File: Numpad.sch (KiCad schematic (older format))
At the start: 68 parts, among them J1 SWD, J2 USB4085-GF-A_REVA, SW1 SW_Push, SW10 SW_Push, SW11 SW_Push, SW12 SW_Push, SW13 SW_Push, SW14 SW_Push, SW15 SW_Push, SW16 SW_Push, SW17 SW_Push, SW18 SW_Push, SW19 SW_Push, SW2 SW_Push, SW20 SW_Push, SW21 SW_Push, SW3 SW_Push, SW4 SW_Push, SW5 SW_Push, SW6 SW_Push, SW7 SW_Push, SW8 SW_Push, SW9 SW_Push, U1 SRV05-4, U2 STM32F103C8Tx, U3 XC6206PxxxMR, Y1 8MHz

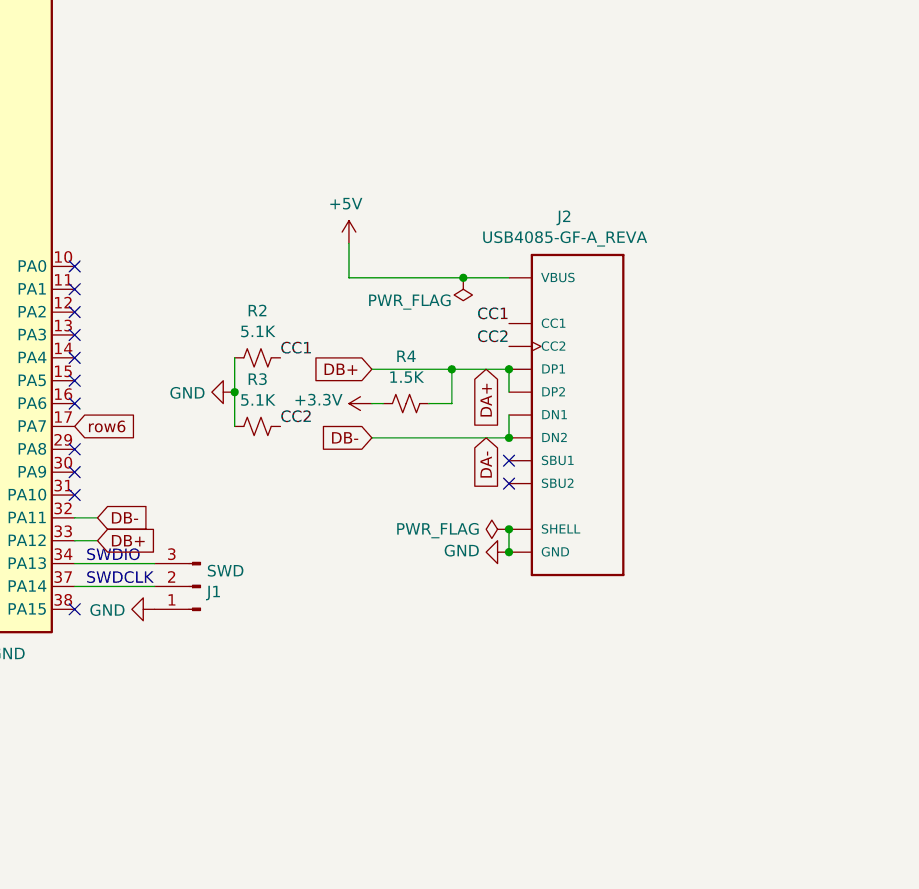
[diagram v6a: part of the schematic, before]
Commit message: 0.3: removed dependencies on external libraries
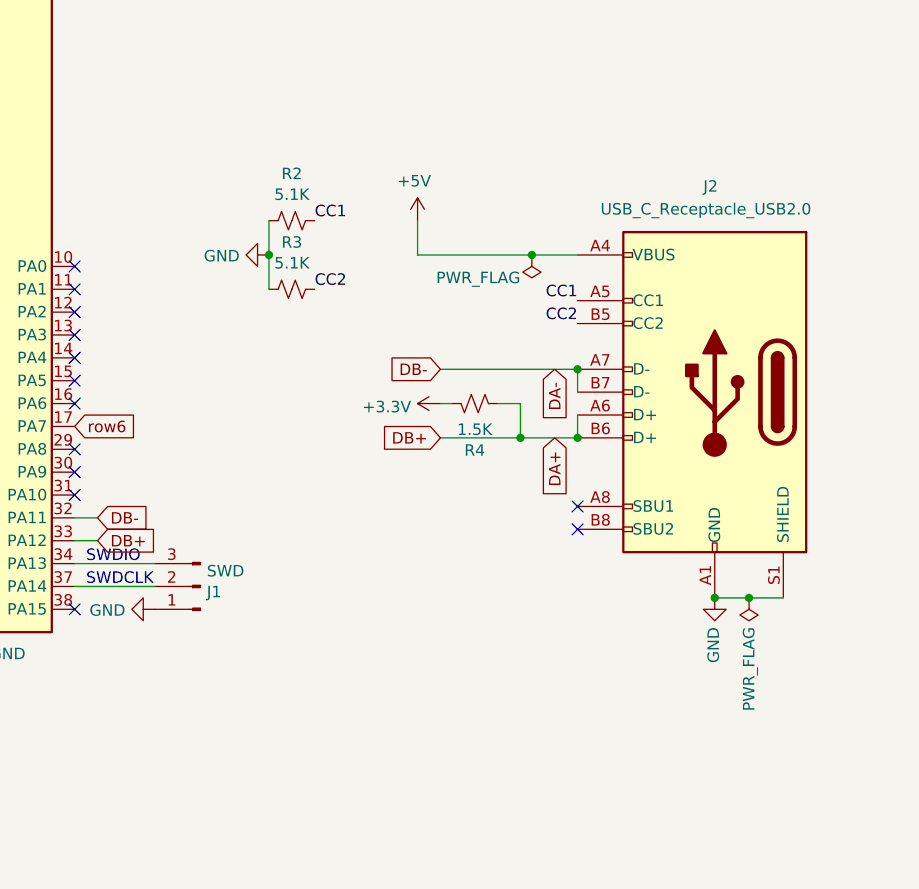
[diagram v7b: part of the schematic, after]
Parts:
- removed J2: USB4085-GF-A_REVA, USB4085:GCT_USB4085-GF-A_REVA, symbol USB4085:USB4085-GF-A_REVA
- added J2: USB_C_Receptacle_USB2.0, Connector_USB:USB_C_Receptacle_GCT_USB4085, symbol Connector:USB_C_Receptacle_USB2.0
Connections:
- net +5V: now also J2.A4 (VBUS), J2.A9 (VBUS), J2.B4 (VBUS), J2.B9 (VBUS)
- net CC1: now also J2.A5 (CC1)
- net CC2: now also J2.B5 (CC2)
- net DA+: now also J2.A6 (D+), J2.B6 (D+)
- net DA-: now also J2.A7 (D-), J2.B7 (D-)
- net GND: now also J2.A1 (GND), J2.A12 (GND), J2.B1 (GND), J2.B12 (GND), J2.S1 (SHIELD)
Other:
- moved on the sheet: R2, R3, R4
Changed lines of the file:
@@
 Text Notes 7700 4600 0    50   ~ 0
 SWDCLK
-$Comp
-L USB4085:USB4085-GF-A_REVA J2
-U 1 1 5E3F05FE
-P 9850 3850
-F 0 "J2" H 9793 4717 50  0000 C CNN
-F 1 "USB4085-GF-A_REVA" H 9793 4626 50  0000 C CNN
-F 2 "USB4085:GCT_USB4085-GF-A_REVA" H 9850 3850 50  0001 L BNN
-F 3 "Global Connector Technology" H 9850 3850 50  0001 L BNN
-F 4 "A" H 9850 3850 50  0001 L BNN "Field4"
-F 5 "Manufacturer Recommendations" H 9850 3850 50  0001 L BNN "Field5"
-	1    9850 3850
-	1    0    0    -1
-$EndComp
-Wire Wire Line
-	8850 3250 8850 3100
+Wire Wire Line
+	9150 3150 9150 3000
 $Comp
 L power:+5V #PWR020
 U 1 1 5E4261EB
-P 8850 3100
-F 0 "#PWR020" H 8850 2950 50  0001 C CNN
-F 1 "+5V" H 8865 3273 50  0000 C CNN
-F 2 "" H 8850 3100 50  0001 C CNN
-F 3 "" H 8850 3100 50  0001 C CNN
-	1    8850 3100
+P 9150 3000
+F 0 "#PWR020" H 9150 2850 50  0001 C CNN
+F 1 "+5V" H 9165 3173 50  0000 C CNN
+F 2 "" H 9150 3000 50  0001 C CNN
+F 3 "" H 9150 3000 50  0001 C CNN
+	1    9150 3000
 	-1   0    0    -1
 $EndComp
-Wire Wire Line
-	9550 3650 9550 3750
-Wire Wire Line
-	9550 3850 9550 3950
 $Comp
 L power:GND #PWR022
 U 1 1 5E42FBA1
-P 9550 4450
-F 0 "#PWR022" H 9550 4200 50  0001 C CNN
-F 1 "GND" V 9555 4322 50  0000 R CNN
-F 2 "" H 9550 4450 50  0001 C CNN
-F 3 "" H 9550 4450 50  0001 C CNN
-	1    9550 4450
-	0    1    -1   0
+P 10450 4650
+F 0 "#PWR022" H 10450 4400 50  0001 C CNN
+F 1 "GND" V 10455 4522 50  0000 R CNN
+F 2 "" H 10450 4650 50  0001 C CNN
+F 3 "" H 10450 4650 50  0001 C CNN
+	1    10450 4650
+	-1   0    0    -1
 $EndComp
 $Comp
 L Device:R_Small_US R2
 U 1 1 5E4574F8
-P 8450 3600
-F 0 "R2" V 8245 3600 50  0000 C CNN
-F 1 "5.1K" V 8336 3600 50  0000 C CNN
-F 2 "Resistor_SMD:R_0402_1005Metric" H 8450 3600 50  0001 C CNN
-F 3 "~" H 8450 3600 50  0001 C CNN
-F 4 "C25905" H 8450 3600 50  0001 C CNN "LCSC"
-	1    8450 3600
+P 8600 3000
+F 0 "R2" V 8395 3000 50  0000 C CNN
+F 1 "5.1K" V 8486 3000 50  0000 C CNN
+F 2 "Resistor_SMD:R_0402_1005Metric" H 8600 3000 50  0001 C CNN
+F 3 "~" H 8600 3000 50  0001 C CNN
+F 4 "C25905" H 8600 3000 50  0001 C CNN "LCSC"
+	1    8600 3000
 	0    1    1    0
 $EndComp
@@
 L power:GND #PWR018
 U 1 1 5E484A5F
-P 8350 3750
-F 0 "#PWR018" H 8350 3500 50  0001 C CNN
-F 1 "GND" V 8355 3622 50  0000 R CNN
-F 2 "" H 8350 3750 50  0001 C CNN
-F 3 "" H 8350 3750 50  0001 C CNN
-	1    8350 3750
+P 8500 3150
+F 0 "#PWR018" H 8500 2900 50  0001 C CNN
+F 1 "GND" V 8505 3022 50  0000 R CNN
+F 2 "" H 8500 3150 50  0001 C CNN
+F 3 "" H 8500 3150 50  0001 C CNN
+	1    8500 3150
 	0    1    1    0
 $EndComp
@@
 NoConn ~ 7650 4100
 NoConn ~ 7650 4200
-NoConn ~ 9550 4050
-NoConn ~ 9550 4150
-Wire Wire Line
-	9550 4350 9550 4450
-Connection ~ 9550 4450
 $Comp
 L Device:R_Small_US R3
 U 1 1 5E458E16
-P 8450 3900
-F 0 "R3" V 8655 3900 50  0000 C CNN
-F 1 "5.1K" V 8564 3900 50  0000 C CNN
-F 2 "Resistor_SMD:R_0402_1005Metric" H 8450 3900 50  0001 C CNN
-F 3 "~" H 8450 3900 50  0001 C CNN
-F 4 "C25905" H 8450 3900 50  0001 C CNN "LCSC"
-	1    8450 3900
+P 8600 3300
+F 0 "R3" V 8805 3300 50  0000 C CNN
+F 1 "5.1K" V 8714 3300 50  0000 C CNN
+F 2 "Resistor_SMD:R_0402_1005Metric" H 8600 3300 50  0001 C CNN
+F 3 "~" H 8600 3300 50  0001 C CNN
+F 4 "C25905" H 8600 3300 50  0001 C CNN "LCSC"
+	1    8600 3300
 	0    -1   -1   0
 $EndComp
@@
 	10200 850  10200 1050
 Wire Wire Line
-	8350 3600 8350 3750
-Wire Wire Line
-	8350 3750 8350 3900
-Connection ~ 8350 3750
-Text Label 8550 3600 0    50   ~ 0
+	8500 3000 8500 3150
+Wire Wire Line
+	8500 3150 8500 3300
+Connection ~ 8500 3150
+Text Label 8700 3000 0    50   ~ 0
 CC1
-Text Label 8550 3900 0    50   ~ 0
+Text Label 8700 3300 0    50   ~ 0
 CC2
-Text Label 9550 3450 2    50   ~ 0
+Text Label 9850 3350 2    50   ~ 0
 CC1
-Text Label 9550 3550 2    50   ~ 0
+Text Label 9850 3450 2    50   ~ 0
 CC2
-Connection ~ 9550 3650
-Connection ~ 9550 3950
 Wire Wire Line
 	7750 4300 7650 4300
@@
 L power:PWR_FLAG #FLG0102
 U 1 1 5E5DCDDC
-P 9550 4350
-F 0 "#FLG0102" H 9550 4425 50  0001 C CNN
-F 1 "PWR_FLAG" V 9550 4477 50  0000 L CNN
-F 2 "" H 9550 4350 50  0001 C CNN
-F 3 "~" H 9550 4350 50  0001 C CNN
-	1    9550 4350
-	0    -1   -1   0
-$EndComp
-Connection ~ 9550 4350
+P 10600 4650
+F 0 "#FLG0102" H 10600 4725 50  0001 C CNN
+F 1 "PWR_FLAG" V 10600 4777 50  0000 L CNN
+F 2 "" H 10600 4650 50  0001 C CNN
+F 3 "~" H 10600 4650 50  0001 C CNN
+	1    10600 4650
+	-1   0    0    1
+$EndComp
 $Comp
 L power:PWR_FLAG #FLG0101
 U 1 1 5E5DC168
-P 9350 3250
-F 0 "#FLG0101" H 9350 3325 50  0001 C CNN
-F 1 "PWR_FLAG" H 9400 3350 50  0000 L CNN
-F 2 "" H 9350 3250 50  0001 C CNN
-F 3 "~" H 9350 3250 50  0001 C CNN
-	1    9350 3250
+P 9650 3150
+F 0 "#FLG0101" H 9650 3225 50  0001 C CNN
+F 1 "PWR_FLAG" H 9700 3250 50  0000 L CNN
+F 2 "" H 9650 3150 50  0001 C CNN
+F 3 "~" H 9650 3150 50  0001 C CNN
+	1    9650 3150
 	-1   0    0    1
 $EndComp
 Wire Wire Line
-	9350 3250 9550 3250
+	9650 3150 9850 3150
 Wire Wire Line
 	6350 2450 6000 2450
@@
 	1    0    0    -1
 $EndComp
-Text GLabel 9450 3650 3    50   Input ~ 0
+Text GLabel 9750 3950 3    50   Input ~ 0
 DA+
-Text GLabel 9450 3950 3    50   Input ~ 0
+Text GLabel 9750 3650 3    50   Input ~ 0
 DA-
-Text GLabel 8950 3650 0    50   Input ~ 0
+Text GLabel 9250 3950 0    50   Input ~ 0
 DB+
-Text GLabel 8950 3950 0    50   Input ~ 0
+Text GLabel 9250 3650 0    50   Input ~ 0
 DB-
 Text GLabel 7750 4300 2    50   Input ~ 0
@@
 DB+
 Wire Wire Line
-	9350 3250 8850 3250
-Connection ~ 9350 3250
-Wire Wire Line
-	8950 3650 9300 3650
-Wire Wire Line
-	8950 3950 9550 3950
+	9650 3150 9150 3150
+Connection ~ 9650 3150
+Wire Wire Line
+	9250 3950 9600 3950
+Wire Wire Line
+	9250 3650 9850 3650
 $Comp
 L Device:R_Small_US R4
 U 1 1 5E36917C
-P 9100 3800
-F 0 "R4" V 9305 3800 50  0000 C CNN
-F 1 "1.5K" V 9214 3800 50  0000 C CNN
-F 2 "Resistor_SMD:R_0402_1005Metric" H 9100 3800 50  0001 C CNN
-F 3 "~" H 9100 3800 50  0001 C CNN
-F 4 "C25867" H 9100 3800 50  0001 C CNN "LCSC"
-	1    9100 3800
-	0    -1   -1   0
-$EndComp
-Wire Wire Line
-	9200 3800 9300 3800
-Wire Wire Line
-	9300 3800 9300 3650
-Connection ~ 9300 3650
-Wire Wire Line
-	9300 3650 9550 3650
-Wire Wire Line
-	9000 3800 8950 3800
+P 9400 3800
+F 0 "R4" V 9605 3800 50  0000 C CNN
+F 1 "1.5K" V 9514 3800 50  0000 C CNN
+F 2 "Resistor_SMD:R_0402_1005Metric" H 9400 3800 50  0001 C CNN
+F 3 "~" H 9400 3800 50  0001 C CNN
+F 4 "C25867" H 9400 3800 50  0001 C CNN "LCSC"
+	1    9400 3800
+	0    -1   1    0
+$EndComp
+Wire Wire Line
+	9500 3800 9600 3800
+Wire Wire Line
+	9600 3800 9600 3950
+Connection ~ 9600 3950
+Wire Wire Line
+	9600 3950 9850 3950
+Wire Wire Line
+	9300 3800 9250 3800
 $Comp
 L power:+3.3V #PWR0101
 U 1 1 5E37570D
-P 8950 3800
-F 0 "#PWR0101" H 8950 3650 50  0001 C CNN
-F 1 "+3.3V" V 8965 3928 50  0000 L CNN
-F 2 "" H 8950 3800 50  0001 C CNN
-F 3 "" H 8950 3800 50  0001 C CNN
-	1    8950 3800
-	0    -1   -1   0
-$EndComp
+P 9250 3800
+F 0 "#PWR0101" H 9250 3650 50  0001 C CNN
+F 1 "+3.3V" V 9265 3928 50  0000 L CNN
+F 2 "" H 9250 3800 50  0001 C CNN
+F 3 "" H 9250 3800 50  0001 C CNN
+	1    9250 3800
+	0    -1   1    0
+$EndComp
+$Comp
+L Connector:USB_C_Receptacle_USB2.0 J2
+U 1 1 5E32AB8D
+P 10450 3750
+F 0 "J2" H 10500 4650 50  0000 R CNN
+F 1 "USB_C_Receptacle_USB2.0" H 10950 4550 50  0000 R CNN
+F 2 "Connector_USB:USB_C_Receptacle_GCT_USB4085" H 10600 3750 50  0001 C CNN
+F 3 "https://www.usb.org/sites/default/files/documents/usb_type-c.zip" H 10600 3750 50  0001 C CNN
+	1    10450 3750
+	-1   0    0    -1
+$EndComp
+Wire Wire Line
+	10450 4650 10600 4650
+Connection ~ 10450 4650
+Connection ~ 10600 4650
+Wire Wire Line
+	10600 4650 10750 4650
+NoConn ~ 9850 4250
+NoConn ~ 9850 4350
+Wire Wire Line
+	9850 3750 9850 3650
+Connection ~ 9850 3650
+Wire Wire Line
+	9850 3850 9850 3950
+Connection ~ 9850 3950
 $EndSCHEMATC

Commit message: v0.4
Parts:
- removed H1, H2, H3, H4: MountingHole_Pad, MountingHole:MountingHole_3.2mm_M3_Pad, symbol Mechanical:MountingHole_Pad
- added H1, H2, H3, H4: MountingHole, MountingHole:MountingHole_3.2mm_M3, symbol Mechanical:MountingHole
- SW_0: renamed from SW6; footprint Button_Switch_Keyboard:SW_Cherry_MX_2.00u_PCB -> Keebio-Parts:MX-Alps-Choc-2U
- SW_1: renamed from SW5; footprint Button_Switch_Keyboard:SW_Cherry_MX_1.00u_PCB -> Keebio-Parts:MX-Alps-Choc-1U
- SW_2: renamed from SW11; footprint Button_Switch_Keyboard:SW_Cherry_MX_1.00u_PCB -> Keebio-Parts:MX-Alps-Choc-1U
- SW_3: renamed from SW16; footprint Button_Switch_Keyboard:SW_Cherry_MX_1.00u_PCB -> Keebio-Parts:MX-Alps-Choc-1U
- SW_4: renamed from SW4; footprint Button_Switch_Keyboard:SW_Cherry_MX_1.00u_PCB -> Keebio-Parts:MX-Alps-Choc-1U
- SW_5: renamed from SW10; footprint Button_Switch_Keyboard:SW_Cherry_MX_1.00u_PCB -> Keebio-Parts:MX-Alps-Choc-1U
- SW_6: renamed from SW15; footprint Button_Switch_Keyboard:SW_Cherry_MX_1.00u_PCB -> Keebio-Parts:MX-Alps-Choc-1U
- SW_7: renamed from SW3; footprint Button_Switch_Keyboard:SW_Cherry_MX_1.00u_PCB -> Keebio-Parts:MX-Alps-Choc-1U
- SW_8: renamed from SW9; footprint Button_Switch_Keyboard:SW_Cherry_MX_1.00u_PCB -> Keebio-Parts:MX-Alps-Choc-1U
- SW_9: renamed from SW14; footprint Button_Switch_Keyboard:SW_Cherry_MX_1.00u_PCB -> Keebio-Parts:MX-Alps-Choc-1U
- SW_BKSP1: renamed from SW18; footprint Button_Switch_Keyboard:SW_Cherry_MX_1.00u_PCB -> Keebio-Parts:MX-Alps-Choc-1U
- SW_DOT1: renamed from SW17; footprint Button_Switch_Keyboard:SW_Cherry_MX_1.00u_PCB -> Keebio-Parts:MX-Alps-Choc-1U
- SW_ENTER1: renamed from SW21; footprint Button_Switch_Keyboard:SW_Cherry_MX_2.00u_Vertical_PCB -> Keebio-Parts:MX-Alps-Choc-2U
- SW_ESC1: renamed from SW1; footprint Button_Switch_Keyboard:SW_Cherry_MX_1.00u_PCB -> Keebio-Parts:MX-Alps-Choc-1U
- SW_FN1: renamed from SW12; footprint Button_Switch_Keyboard:SW_Cherry_MX_1.00u_PCB -> Keebio-Parts:MX-Alps-Choc-1U
- SW_MINUS1: renamed from SW19; footprint Button_Switch_Keyboard:SW_Cherry_MX_1.00u_PCB -> Keebio-Parts:MX-Alps-Choc-1U
- SW_NUMLK1: renamed from SW2; footprint Button_Switch_Keyboard:SW_Cherry_MX_1.00u_PCB -> Keebio-Parts:MX-Alps-Choc-1U
- SW_PLUS1: renamed from SW20; footprint Button_Switch_Keyboard:SW_Cherry_MX_2.00u_Vertical_PCB -> Keebio-Parts:MX-Alps-Choc-2U
- SW_SLASH1: renamed from SW8; footprint Button_Switch_Keyboard:SW_Cherry_MX_1.00u_PCB -> Keebio-Parts:MX-Alps-Choc-1U
- SW_STAR1: renamed from SW13; footprint Button_Switch_Keyboard:SW_Cherry_MX_1.00u_PCB -> Keebio-Parts:MX-Alps-Choc-1U
- SW_TAB1: renamed from SW7; footprint Button_Switch_Keyboard:SW_Cherry_MX_1.00u_PCB -> Keebio-Parts:MX-Alps-Choc-1U
- renumbered D6 to D_0, D5 to D_1, D11 to D_2, D16 to D_3, D4 to D_4, D10 to D_5, D15 to D_6, D3 to D_7, D9 to D_8, D14 to D_9, D18 to D_BKSP1, D17 to D_DOT1, D21 to D_ENTER1, D1 to D_ESC1, D12 to D_FN1, D19 to D_MINUS1, D2 to D_NUMLK1, D20 to D_PLUS1, D8 to D_SLASH1, D13 to D_STAR1, D7 to D_TAB1
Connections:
- net col1: now also SW_0.1, SW_1.1, SW_4.1, SW_7.1, SW_ESC1.1, SW_NUMLK1.1, U2.26 (PB13); no longer D_0.1 (K), D_1.1 (K), D_4.1 (K), D_7.1 (K), D_ESC1.1 (K), D_NUMLK1.1 (K), U2.28 (PB15)
- net col2: now also SW_2.1, SW_5.1, SW_8.1, SW_SLASH1.1, SW_TAB1.1, U2.25 (PB12); no longer D_2.1 (K), D_5.1 (K), D_8.1 (K), D_SLASH1.1 (K), D_TAB1.1 (K), U2.27 (PB14)
- net col3: now also SW_3.1, SW_6.1, SW_9.1, SW_DOT1.1, SW_FN1.1, SW_STAR1.1, U2.13 (PA3); no longer D_3.1 (K), D_6.1 (K), D_9.1 (K), D_DOT1.1 (K), D_FN1.1 (K), D_STAR1.1 (K), U2.26 (PB13)
- net col4: now also SW_BKSP1.1, SW_ENTER1.1, SW_MINUS1.1, SW_PLUS1.1, U2.12 (PA2); no longer D_BKSP1.1 (K), D_ENTER1.1 (K), D_MINUS1.1 (K), D_PLUS1.1 (K), U2.25 (PB12)
- net row1: now also D_BKSP1.1 (K), D_ESC1.1 (K), D_FN1.1 (K), D_TAB1.1 (K), U2.46 (PB9); no longer SW_BKSP1.2, SW_ESC1.2, SW_FN1.2, SW_TAB1.2, U2.22 (PB11)
- net row2: now also D_MINUS1.1 (K), D_NUMLK1.1 (K), D_SLASH1.1 (K), D_STAR1.1 (K); no longer SW_MINUS1.2, SW_NUMLK1.2, SW_SLASH1.2, SW_STAR1.2
- net row3: now also D_7.1 (K), D_8.1 (K), D_9.1 (K), D_PLUS1.1 (K), U2.22 (PB11); no longer SW_7.2, SW_8.2, SW_9.2, SW_PLUS1.2, U2.20 (PB2)
- net row4: now also D_4.1 (K), D_5.1 (K), D_6.1 (K); no longer SW_4.2, SW_5.2, SW_6.2
- net row5: now also D_1.1 (K), D_2.1 (K), D_3.1 (K), D_ENTER1.1 (K); no longer SW_1.2, SW_2.2, SW_3.2, SW_ENTER1.2
- net row6: now also D_0.1 (K), D_DOT1.1 (K); no longer SW_0.2, SW_DOT1.2
- net at D_ESC1.2 (A): now also SW_ESC1.2; no longer SW_ESC1.1
- net at D_TAB1.2 (A): now also SW_TAB1.2; no longer SW_TAB1.1
- net at D_FN1.2 (A): now also SW_FN1.2; no longer SW_FN1.1
- net at D_BKSP1.2 (A): now also SW_BKSP1.2; no longer SW_BKSP1.1
- net at D_NUMLK1.2 (A): now also SW_NUMLK1.2; no longer SW_NUMLK1.1
- net at D_SLASH1.2 (A): now also SW_SLASH1.2; no longer SW_SLASH1.1
- net at D_STAR1.2 (A): now also SW_STAR1.2; no longer SW_STAR1.1
- net at D_MINUS1.2 (A): now also SW_MINUS1.2; no longer SW_MINUS1.1
- net at D_7.2 (A): now also SW_7.2; no longer SW_7.1
- net at D_8.2 (A): now also SW_8.2; no longer SW_8.1
- net at D_9.2 (A): now also SW_9.2; no longer SW_9.1
- net at D_4.2 (A): now also SW_4.2; no longer SW_4.1
- net at D_5.2 (A): now also SW_5.2; no longer SW_5.1
- net at D_6.2 (A): now also SW_6.2; no longer SW_6.1
- net at D_PLUS1.2 (A): now also SW_PLUS1.2; no longer SW_PLUS1.1
- net at D_1.2 (A): now also SW_1.2; no longer SW_1.1
- net at D_2.2 (A): now also SW_2.2; no longer SW_2.1
- net at D_3.2 (A): now also SW_3.2; no longer SW_3.1
- net at D_0.2 (A): now also SW_0.2; no longer SW_0.1
- net at D_DOT1.2 (A): now also SW_DOT1.2; no longer SW_DOT1.1
- net at D_ENTER1.2 (A): now also SW_ENTER1.2; no longer SW_ENTER1.1
- no-connect marks 25 -> 20
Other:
- moved on the sheet: D_0, D_1, D_2, D_3, D_4, D_5, D_6, D_7, D_8, D_9, D_BKSP1, D_DOT1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
